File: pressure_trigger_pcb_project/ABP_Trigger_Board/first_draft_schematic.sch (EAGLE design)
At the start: 27 parts, among them U1 AD5206BRUZ10, U2 OPA4340UA

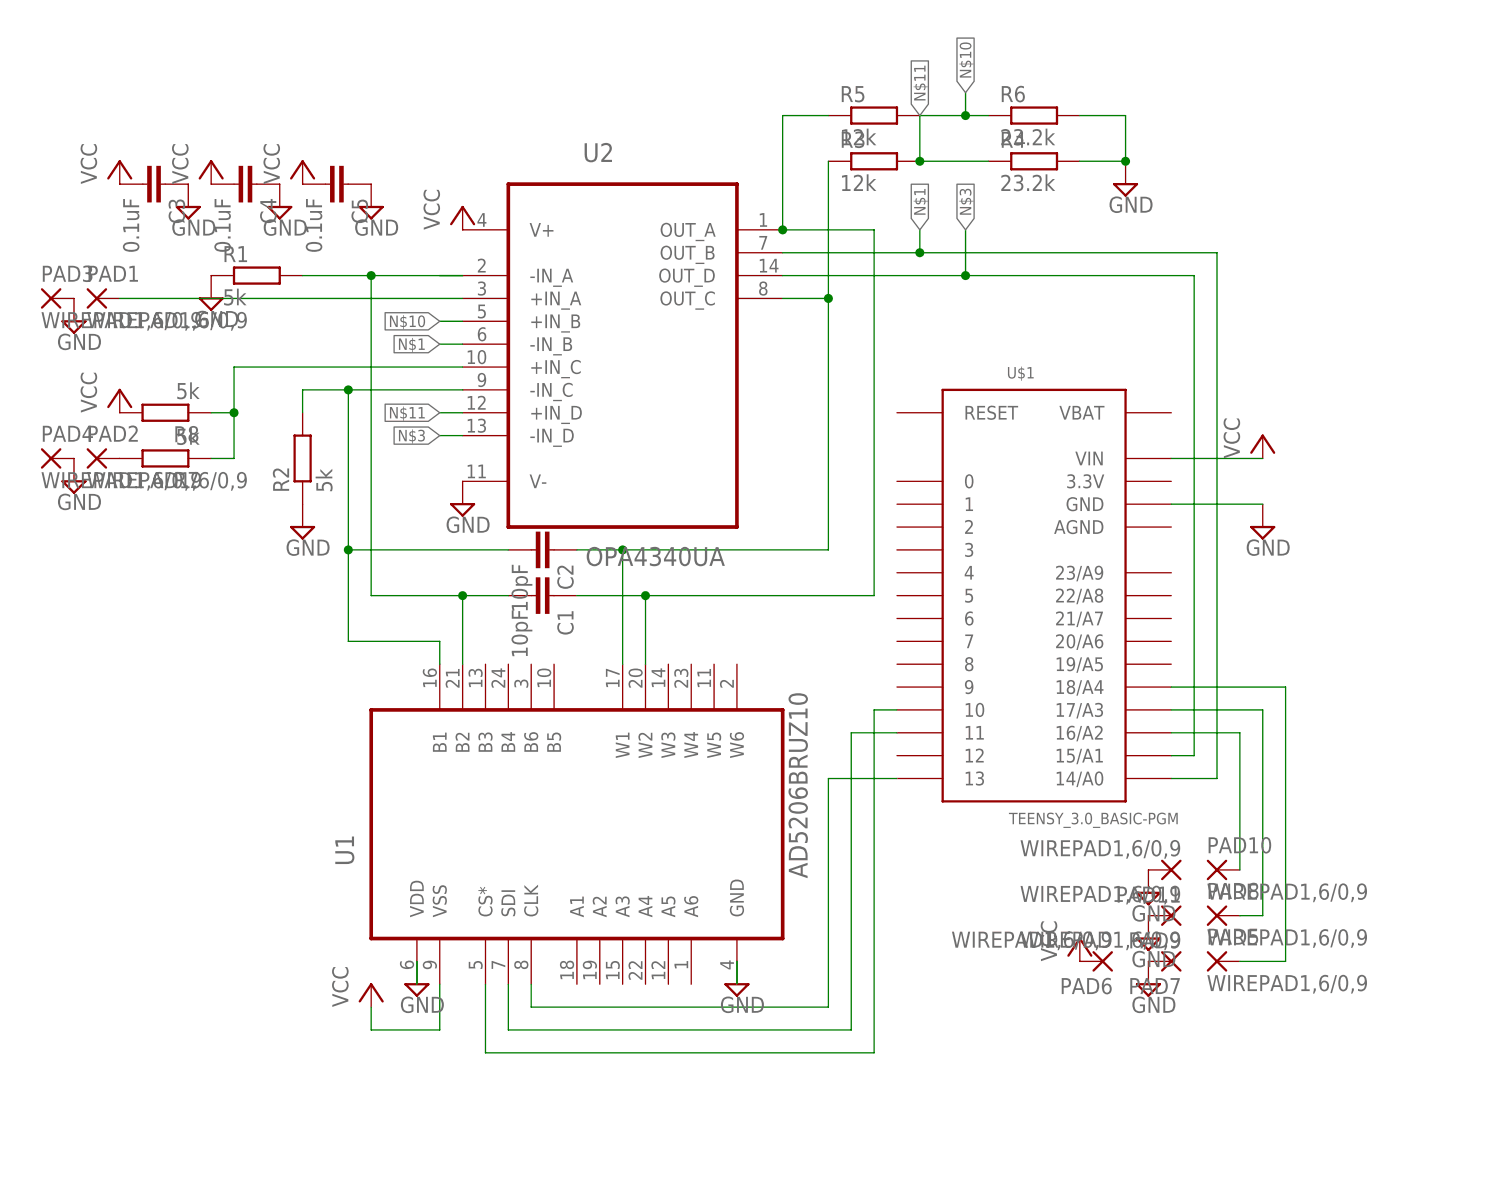
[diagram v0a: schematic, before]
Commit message: routed REV A of the board, silkscreen not yet done
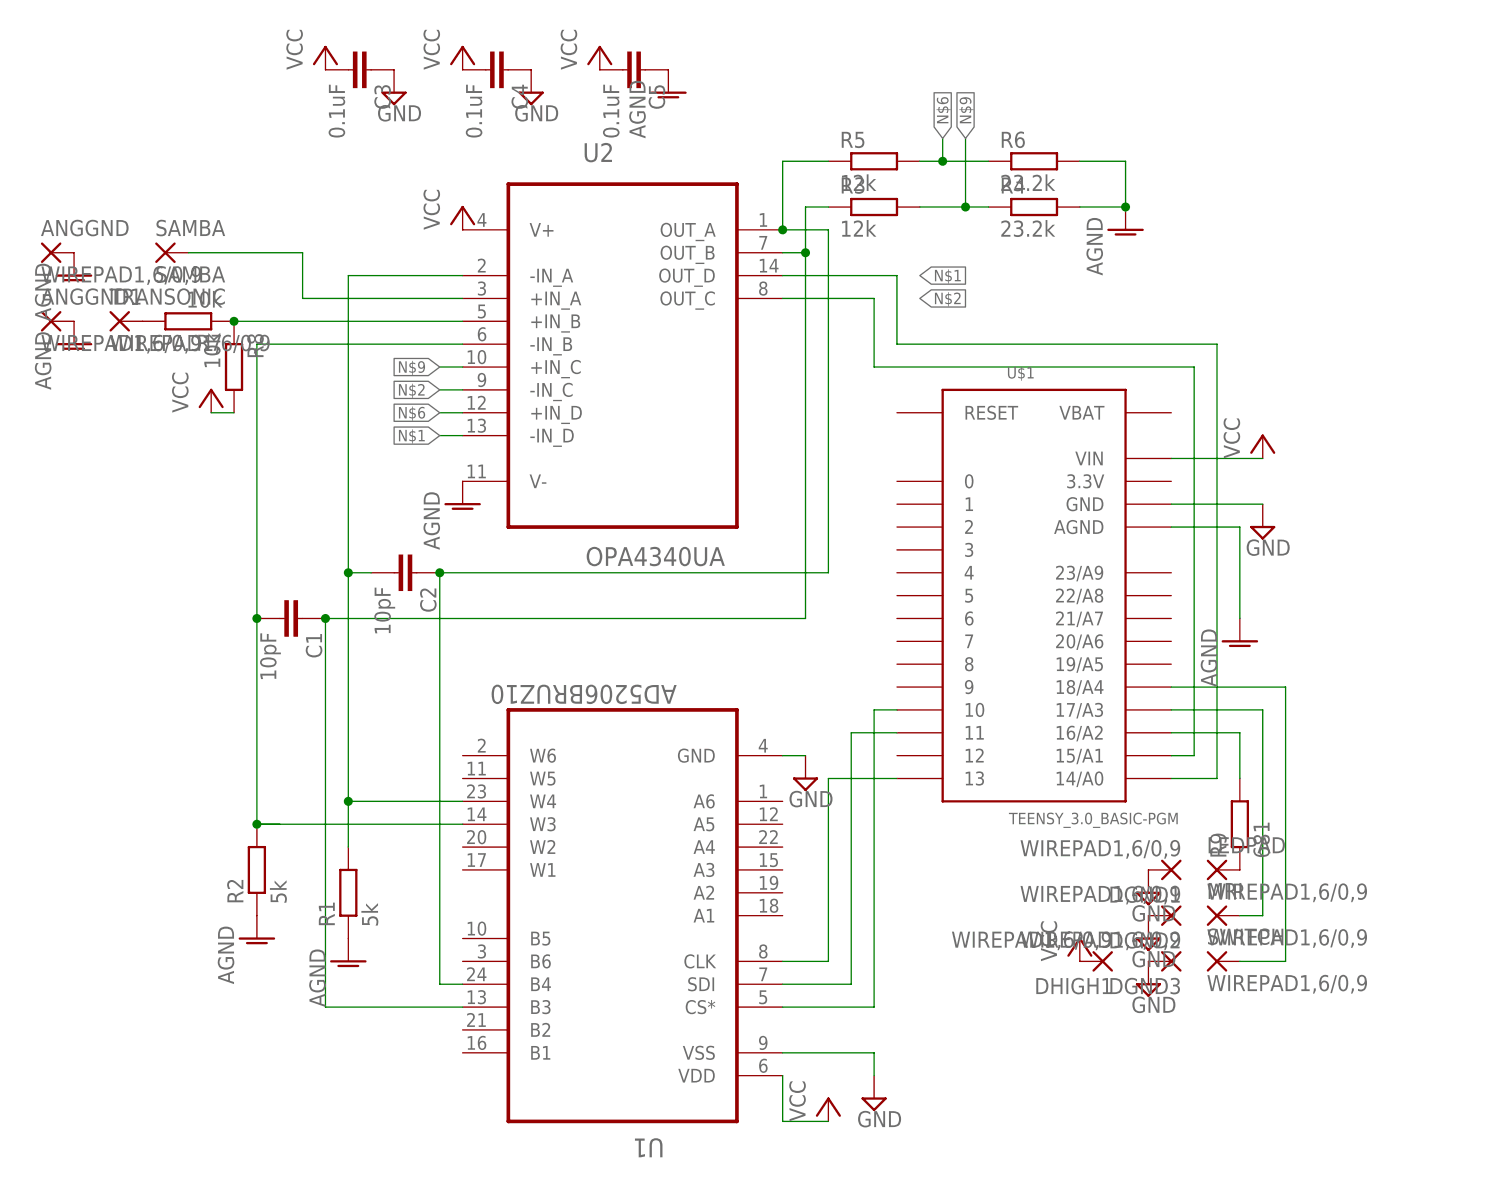
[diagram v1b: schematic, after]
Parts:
- removed PAD1, PAD2, PAD3, PAD4: WIREPAD1,6/0,9, wirepad:WIREPAD1,6/0,9
- added ANGGND, ANGGND1, TRANSONIC: WIREPAD1,6/0,9, wirepad:WIREPAD1,6/0,9
- added R9: 681, resistor:R-EU_R0805
- added SAMBA: SAMBA, wirepad:WIREPAD1,6/0,9
- R7, R8: value 5k -> 10k
- renumbered PAD10 to LEDPAD, PAD11 to DGND1, PAD5 to SWITCH, PAD6 to DHIGH1, PAD7 to DGND3, PAD8 to MRI, PAD9 to DGND2
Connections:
- new net AGND: ANGGND.P, ANGGND1.P, C5.1, R1.1, R2.1, R4.2, R6.2, U$1.AGND, U2.V-
- new net N$9: R3.2, R4.1, U2.+IN_C
- net GND: now also U1.VSS; no longer C5.1, PAD3.P, PAD4.P, R1.1, R2.1, R4.2, R6.2, U1.VDD, U2.V-
- net N$1: now also U2.-IN_D, U2.OUT_D; no longer U2.-IN_B, U2.OUT_B
- net N$10: now also SAMBA.P, U2.+IN_A; no longer R5.2, R6.1, U2.+IN_B
- net N$11: now also LEDPAD.P, R9.1; no longer R3.2, R4.1, U2.+IN_D
- net N$12: now also C1.2, R2.2, U1.W3, U2.-IN_B; no longer PAD1.P, U2.+IN_A
- net N$13: now also TRANSONIC.P; no longer PAD2.P
- net N$14: now also R9.2; no longer LEDPAD.P
- net N$17: now also C1.1, R3.1, U1.B3, U2.OUT_B; no longer R7.1, R8.1, U2.+IN_C
- net N$2: now also U$1.15/A1, U2.OUT_C; no longer C2.2, R2.2, U1.B1
- net N$3: now also C2.2, R1.2, U1.W4, U2.-IN_A; no longer U$1.15/A1, U2.-IN_D, U2.OUT_D
- net N$4: now also R7.1, R8.1, U2.+IN_B; no longer C1.1, R5.1, U1.W2, U2.OUT_A
- net N$5: now also R5.1, U1.B4, U2.OUT_A; no longer R3.1, U1.W1, U2.OUT_C
- net N$6: now also R5.2, R6.1, U2.+IN_D; no longer C1.2, R1.2, U1.B2, U2.-IN_A
- net VCC: now also U1.VDD; no longer U1.VSS
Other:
- moved on the sheet: C1, C2, C3, C4, C5, R1, R2, R3, R4, R5, R6, R7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

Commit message: updated board fixed labels
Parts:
- removed U2: OPA4340UA, Texas Instruments_By_element14_Batch_1:OPA4340UA
- added AD5206: AD5206BRUZ10, AD5206:AD5206BRUZ10
- C2: value 10pF -> 0.1uF
- C3: value 0.1uF -> 10pF
- R1, R2: value 5k -> 10k
- R3: value 12k -> 5k
- R4: value 23.2k -> 5k
- R6: value 23.2k -> 12k
- R7, R8: value 10k -> 23.2k
- U1: value AD5206BRUZ10 -> OPA4340UA; device AD5206:AD5206BRUZ10 -> Texas Instruments_By_element14_Batch_1:OPA4340UA
- renumbered ANGGND to PAD1, ANGGND1 to PAD2, DGND1 to PAD6, DGND2 to PAD7, DGND3 to PAD8, DHIGH1 to PAD5, LEDPAD to PAD9, MRI to PAD10, SAMBA to PAD4, SWITCH to PAD11, TRANSONIC to PAD3, U$1 to TEENSY3.0
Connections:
- net AGND: now also R3.1, R4.1, R7.2, R8.2, U1.V-; no longer R1.1, R2.1, R4.2, R6.2, U2.V-
- net GND: now also AD5206.GND, AD5206.VSS, C2.1; no longer C3.1, U1.GND, U1.VSS
- net N$1: now also U1.-IN_D, U1.OUT_D; no longer U2.-IN_D, U2.OUT_D
- net N$10: now also U1.+IN_A; no longer U2.+IN_A
- net N$12: now also AD5206.W3, R3.2, U1.-IN_B; no longer R2.2, U1.W3, U2.-IN_B
- net N$13: now also R1.2; no longer R7.2
- net N$17: now also AD5206.B3, R6.1, U1.OUT_B; no longer R3.1, U1.B3, U2.OUT_B
- net N$19: now also AD5206.CLK; no longer U1.CLK
- net N$2: now also U1.-IN_C, U1.OUT_C; no longer U2.-IN_C, U2.OUT_C
- net N$3: now also AD5206.W4, C3.2, R4.2, U1.-IN_A; no longer C2.2, R1.2, U1.W4, U2.-IN_A
- net N$4: now also R1.1, R2.1, U1.+IN_B; no longer R7.1, R8.1, U2.+IN_B
- net N$5: now also AD5206.B4, C3.1, U1.OUT_A; no longer C2.1, U1.B4, U2.OUT_A
- net N$6: now also R7.1, U1.+IN_D; no longer R6.1, U2.+IN_D
- net N$7: now also AD5206.CS*; no longer U1.CS*
- net N$8: now also AD5206.SDI; no longer U1.SDI
- net N$9: now also R6.2, R8.1, U1.+IN_C; no longer R3.2, R4.1, U2.+IN_C
- net VCC: now also AD5206.VDD, C2.2, R2.2, U1.V+; no longer C3.2, R8.2, U1.VDD, U2.V+
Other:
- moved on the sheet: C2, C3, R1, R2, R3, R4, R6, R7, R8

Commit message: new board layout
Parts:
- renumbered AD5206 to AD5206-50, PAD1 to TG, PAD10 to MRI, PAD11 to SEL, PAD2 to SG, PAD3 to TC, PAD4 to SB, PAD5 to DH, PAD9 to LED
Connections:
- net N$1: now also TEENSY3.0.15/A1; no longer TEENSY3.0.14/A0
- net N$2: now also TEENSY3.0.14/A0; no longer TEENSY3.0.15/A1

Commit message: schematic before package switch
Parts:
- removed LED: WIREPAD1,6/0,9, wirepad:WIREPAD1,6/0,9
- added L1, L2, LED2, PAD1, PAD2: WIREPAD1,6/0,9, wirepad:WIREPAD1,6/0,9
- added R10, R11: 681, resistor:R-EU_R0805
- renumbered TEENSY3.0 to TEENSY3.0-MICROCONTROLLER
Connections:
- new net N$18: L1.P, R10.1
- new net N$21: R10.2, TEENSY3.0-MICROCONTROLLER.19/A5
- new net N$22: LED2.P, R11.1
- new net N$23: R11.2, TEENSY3.0-MICROCONTROLLER.20/A6
- net GND: now also PAD1.P, PAD2.P
- net N$11: now also L2.P; no longer LED.P
- net N$14: now also TEENSY3.0-MICROCONTROLLER.18/A4; no longer TEENSY3.0-MICROCONTROLLER.16/A2
- net N$15: now also TEENSY3.0-MICROCONTROLLER.16/A2; no longer TEENSY3.0-MICROCONTROLLER.17/A3
- net N$16: now also TEENSY3.0-MICROCONTROLLER.17/A3; no longer TEENSY3.0-MICROCONTROLLER.18/A4
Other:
- moved on the sheet: PAD6, R9

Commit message: finalized board layout
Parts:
- removed AD5206-50: AD5206BRUZ10, AD5206:AD5206BRUZ10
- added U2: AD5206BRUZ10SOIC24R, AD5206_SOIC:AD5206BRUZ10SOIC24R
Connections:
- net GND: now also U2.GND, U2.VSS; no longer AD5206-50.GND, AD5206-50.VSS
- net N$12: now also U2.W3; no longer AD5206-50.W3
- net N$17: now also U2.B3; no longer AD5206-50.B3
- net N$19: now also U2.CLK; no longer AD5206-50.CLK
- net N$3: now also U2.W4; no longer AD5206-50.W4
- net N$5: now also U2.B4; no longer AD5206-50.B4
- net N$7: now also U2.CS*; no longer AD5206-50.CS*
- net N$8: now also U2.SDI; no longer AD5206-50.SDI
- net VCC: now also U2.VDD; no longer AD5206-50.VDD
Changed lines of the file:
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@@
 <parts>
 <part name="TEENSY3.0-MICROCONTROLLER" library="Teensy3.0" deviceset="TEENSY_3.0_BASIC-PGM" device=""/>
-<part name="AD5206-50" library="AD5206" deviceset="AD5206BRUZ10" device=""/>
 <part name="U1" library="Texas Instruments_By_element14_Batch_1" deviceset="OPA4340UA" device=""/>
 <part name="R4" library="resistor" deviceset="R-EU_" device="R0805" value="5k"/>
@@
 <part name="PAD2" library="wirepad" deviceset="WIREPAD" device="1,6/0,9"/>
 <part name="SUPPLY10" library="supply2" deviceset="GND" device=""/>
+<part name="U2" library="AD5206_SOIC" deviceset="AD5206BRUZ10" device="SOIC24R"/>
 </parts>
 <sheets>
@@
 <attribute name="NAME" x="57.912" y="41.91" size="1.27" layer="95" font="vector" ratio="15"/>
 </instance>
-<instance part="AD5206-50" gate="A" x="15.24" y="30.48" smashed="yes" rot="R180"/>
 <instance part="U1" gate="A" x="15.24" y="99.06" smashed="yes">
 <attribute name="VALUE" x="11.0998" y="71.882" size="2.0828" layer="96" ratio="10" rot="SR0"/>
@@
 </instance>
 <instance part="SUPPLY10" gate="GND" x="106.68" y="50.8" smashed="yes"/>
+<instance part="U2" gate="A" x="15.24" y="30.48" rot="R180"/>
 </instances>
 <busses>
@@
 <pinref part="SUPPLY4" gate="GND" pin="GND"/>
 <wire x1="43.18" y1="15.24" x2="43.18" y2="17.78" width="0.1524" layer="91"/>
-<pinref part="AD5206-50" gate="A" pin="VSS"/>
 <wire x1="43.18" y1="17.78" x2="33.02" y2="17.78" width="0.1524" layer="91"/>
+<pinref part="U2" gate="A" pin="VSS"/>
 </segment>
 <segment>
@@
 </segment>
 <segment>
-<pinref part="AD5206-50" gate="A" pin="GND"/>
 <wire x1="35.56" y1="50.8" x2="33.02" y2="50.8" width="0.1524" layer="91"/>
 <pinref part="SUPPLY3" gate="GND" pin="GND"/>
+<pinref part="U2" gate="A" pin="GND"/>
 </segment>
 <segment>
@@
 </segment>
 <segment>
-<pinref part="AD5206-50" gate="A" pin="VDD"/>
 <wire x1="33.02" y1="15.24" x2="33.02" y2="10.16" width="0.1524" layer="91"/>
 <pinref part="P+6" gate="VCC" pin="VCC"/>
 <wire x1="33.02" y1="10.16" x2="38.1" y2="10.16" width="0.1524" layer="91"/>
+<pinref part="U2" gate="A" pin="VDD"/>
 </segment>
 <segment>
@@
 <net name="N$7" class="0">
 <segment>
-<pinref part="AD5206-50" gate="A" pin="CS*"/>
 <wire x1="33.02" y1="22.86" x2="43.18" y2="22.86" width="0.1524" layer="91"/>
 <wire x1="43.18" y1="22.86" x2="43.18" y2="55.88" width="0.1524" layer="91"/>
 <pinref part="TEENSY3.0-MICROCONTROLLER" gate="G$1" pin="10"/>
 <wire x1="43.18" y1="55.88" x2="45.72" y2="55.88" width="0.1524" layer="91"/>
+<pinref part="U2" gate="A" pin="CS*"/>
 </segment>
 </net>
 <net name="N$8" class="0">
 <segment>
-<pinref part="AD5206-50" gate="A" pin="SDI"/>
 <wire x1="33.02" y1="25.4" x2="40.64" y2="25.4" width="0.1524" layer="91"/>
 <wire x1="40.64" y1="25.4" x2="40.64" y2="53.34" width="0.1524" layer="91"/>
 <pinref part="TEENSY3.0-MICROCONTROLLER" gate="G$1" pin="11"/>
 <wire x1="40.64" y1="53.34" x2="45.72" y2="53.34" width="0.1524" layer="91"/>
+<pinref part="U2" gate="A" pin="SDI"/>
 </segment>
 </net>
@@
 <net name="N$19" class="0">
 <segment>
-<pinref part="AD5206-50" gate="A" pin="CLK"/>
 <wire x1="33.02" y1="27.94" x2="38.1" y2="27.94" width="0.1524" layer="91"/>
 <wire x1="38.1" y1="27.94" x2="38.1" y2="48.26" width="0.1524" layer="91"/>
 <pinref part="TEENSY3.0-MICROCONTROLLER" gate="G$1" pin="13"/>
 <wire x1="38.1" y1="48.26" x2="45.72" y2="48.26" width="0.1524" layer="91"/>
+<pinref part="U2" gate="A" pin="CLK"/>
 </segment>
 </net>
@@
 <wire x1="-2.54" y1="96.52" x2="-25.4" y2="96.52" width="0.1524" layer="91"/>
 <wire x1="-25.4" y1="96.52" x2="-25.4" y2="66.04" width="0.1524" layer="91"/>
-<pinref part="AD5206-50" gate="A" pin="W3"/>
 <wire x1="-25.4" y1="66.04" x2="-25.4" y2="43.18" width="0.1524" layer="91"/>
 <wire x1="-25.4" y1="43.18" x2="-2.54" y2="43.18" width="0.1524" layer="91"/>
@@
 <pinref part="R3" gate="G$1" pin="2"/>
 <wire x1="-22.86" y1="43.18" x2="-25.4" y2="43.18" width="0.1524" layer="91"/>
+<pinref part="U2" gate="A" pin="W3"/>
 </segment>
 </net>
 <net name="N$3" class="0">
 <segment>
-<pinref part="AD5206-50" gate="A" pin="W4"/>
 <wire x1="-15.24" y1="45.72" x2="-2.54" y2="45.72" width="0.1524" layer="91"/>
 <pinref part="U1" gate="A" pin="-IN_A"/>
@@
 <wire x1="-15.24" y1="45.72" x2="-15.24" y2="40.64" width="0.1524" layer="91"/>
 <junction x="-15.24" y="45.72"/>
+<pinref part="U2" gate="A" pin="W4"/>
 </segment>
 </net>
@@
 <pinref part="C1" gate="G$1" pin="1"/>
 <wire x1="-17.78" y1="66.04" x2="-17.78" y2="22.86" width="0.1524" layer="91"/>
-<pinref part="AD5206-50" gate="A" pin="B3"/>
 <wire x1="-17.78" y1="22.86" x2="-2.54" y2="22.86" width="0.1524" layer="91"/>
 <pinref part="U1" gate="A" pin="OUT_B"/>
@@
 <pinref part="R6" gate="G$1" pin="1"/>
 <wire x1="35.56" y1="111.76" x2="38.1" y2="111.76" width="0.1524" layer="91"/>
+<pinref part="U2" gate="A" pin="B3"/>
 </segment>
 </net>
@@
 <wire x1="-5.08" y1="71.12" x2="-5.08" y2="25.4" width="0.1524" layer="91"/>
 <junction x="-5.08" y="71.12"/>
-<pinref part="AD5206-50" gate="A" pin="B4"/>
 <wire x1="-5.08" y1="25.4" x2="-2.54" y2="25.4" width="0.1524" layer="91"/>
 <pinref part="U1" gate="A" pin="OUT_A"/>
@@
 <wire x1="33.02" y1="109.22" x2="33.02" y2="116.84" width="0.1524" layer="91"/>
 <junction x="33.02" y="109.22"/>
-</segment>
-</net>
+<pinref part="U2" gate="A" pin="B4"/>
+</segment>
+</net>
